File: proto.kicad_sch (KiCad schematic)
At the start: 9 parts, among them J5 Conn_01x05, J6 Conn_01x05, J7 Conn_01x03, J8 Conn_01x04

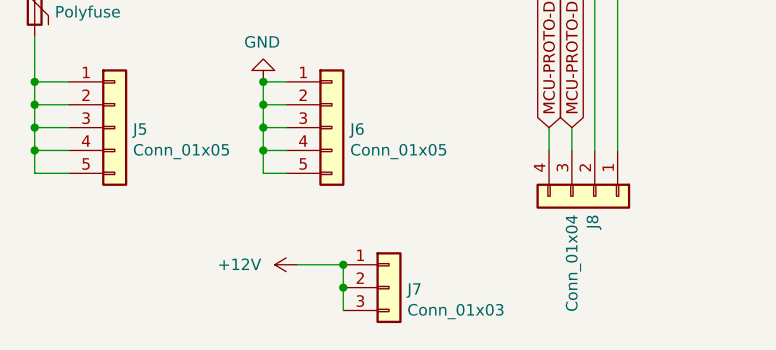
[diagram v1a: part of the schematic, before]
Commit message: Completed layout, slight changes to schematic to optimise routing, 12V proto supply rail removed
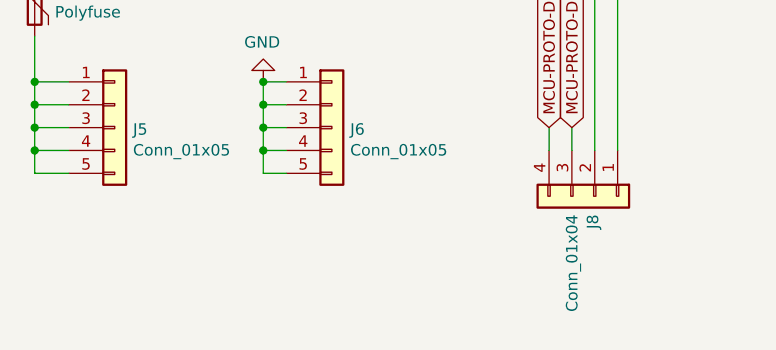
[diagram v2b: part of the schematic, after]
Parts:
- removed J7: Conn_01x03, Connector_PinHeader_2.54mm:PinHeader_1x03_P2.54mm_Vertical, symbol Connector_Generic:Conn_01x03
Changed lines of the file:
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@@
   (junction (at 119.38 96.52) (diameter 0) (color 0 0 0 0)
   )
-  (junction (at 128.27 111.76) (diameter 0) (color 0 0 0 0)
-  )
   (junction (at 119.38 91.44) (diameter 0) (color 0 0 0 0)
   )
-  (junction (at 128.27 109.22) (diameter 0) (color 0 0 0 0)
-  )
   (junction (at 93.98 93.98) (diameter 0) (color 0 0 0 0)
   )
@@
     (stroke (width 0) (type default) (color 0 0 0 0))
   )
-  (wire (pts (xy 128.27 111.76) (xy 128.27 114.3))
-    (stroke (width 0) (type default) (color 0 0 0 0))
-  )
   (wire (pts (xy 156.21 47.625) (xy 156.21 59.055))
     (stroke (width 0) (type default) (color 0 0 0 0))
@@
     (stroke (width 0) (type default) (color 0 0 0 0))
   )
-  (wire (pts (xy 128.27 109.22) (xy 128.27 111.76))
-    (stroke (width 0) (type default) (color 0 0 0 0))
-  )
   (wire (pts (xy 93.98 91.44) (xy 93.98 93.98))
-    (stroke (width 0) (type default) (color 0 0 0 0))
-  )
-  (wire (pts (xy 123.19 109.22) (xy 128.27 109.22))
     (stroke (width 0) (type default) (color 0 0 0 0))
   )
@@
     (pin "1")
   )
-  (symbol (lib_id "Connector_Generic:Conn_01x03") (at 133.35 111.76 0) (unit 1)
-    (in_bom yes) (on_board yes)
-    (property "Reference" "J7" (id 0) (at 135.382 111.9632 0)
-      (effects (font (size 1.27 1.27)) (justify left))
-    )
-    (property "Value" "Conn_01x03" (id 1) (at 135.382 114.2746 0)
-      (effects (font (size 1.27 1.27)) (justify left))
-    )
-    (property "Footprint" "Connector_PinHeader_2.54mm:PinHeader_1x03_P2.54mm_Vertical" (id 2) (at 133.35 111.76 0)
-      (effects (font (size 1.27 1.27)) hide)
-    )
-    (property "Datasheet" "~" (id 3) (at 133.35 111.76 0)
-      (effects (font (size 1.27 1.27)) hide)
-    )
-    (pin "1")
-    (pin "2")
-    (pin "3")
-  )
   (symbol (lib_id "Device:Polyfuse") (at 93.98 80.01 0) (unit 1)
     (in_bom yes) (on_board yes)
@@
       (effects (font (size 1.27 1.27)) hide)
     )
-    (pin "1")
-  )
-  (symbol (lib_id "power:+12V") (at 123.19 109.22 90) (unit 1)
-    (in_bom yes) (on_board yes)
-    (property "Reference" "#PWR0192" (id 0) (at 127 109.22 0)
-      (effects (font (size 1.27 1.27)) hide)
-    )
-    (property "Value" "+12V" (id 1) (at 114.3 109.22 90)
-      (effects (font (size 1.27 1.27)) (justify right))
-    )
-    (property "Footprint" "" (id 2) (at 123.19 109.22 0)
-      (effects (font (size 1.27 1.27)) hide)
-    )
-    (property "Datasheet" "" (id 3) (at 123.19 109.22 0)
-      (effects (font (size 1.27 1.27)) hide)
-    )
